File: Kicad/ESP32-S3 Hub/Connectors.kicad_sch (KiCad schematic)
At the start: 25 parts, among them J1 1.27mm 3pin socket, J10 1.27mm 3pin socket, J11 7 pin FPC 0.3mm Panasonic Y3b, J12 1.27mm 3pin socket, J13 TE 3-2363961-0 receptacle, J14 TE 3-2363962-0 Connector, J16 TE 3-2363961-0 receptacle, J17 TE 3-2363962-0 Connector, J2 1.27mm 3pin socket, J21 1.27mm 4 pin socket, J22 1.27mm 4 pin header, J3 7 pin FPC 0.3mm Panasonic Y3b, J4 1.27mm 3pin socket, J5 7 pin FPC 0.3mm Panasonic Y3b, J6 1.27mm 3pin socket, J7 1.27mm 3pin socket, J8 7 pin FPC 0.3mm Panasonic Y3b, J9 1.27mm 3pin socket

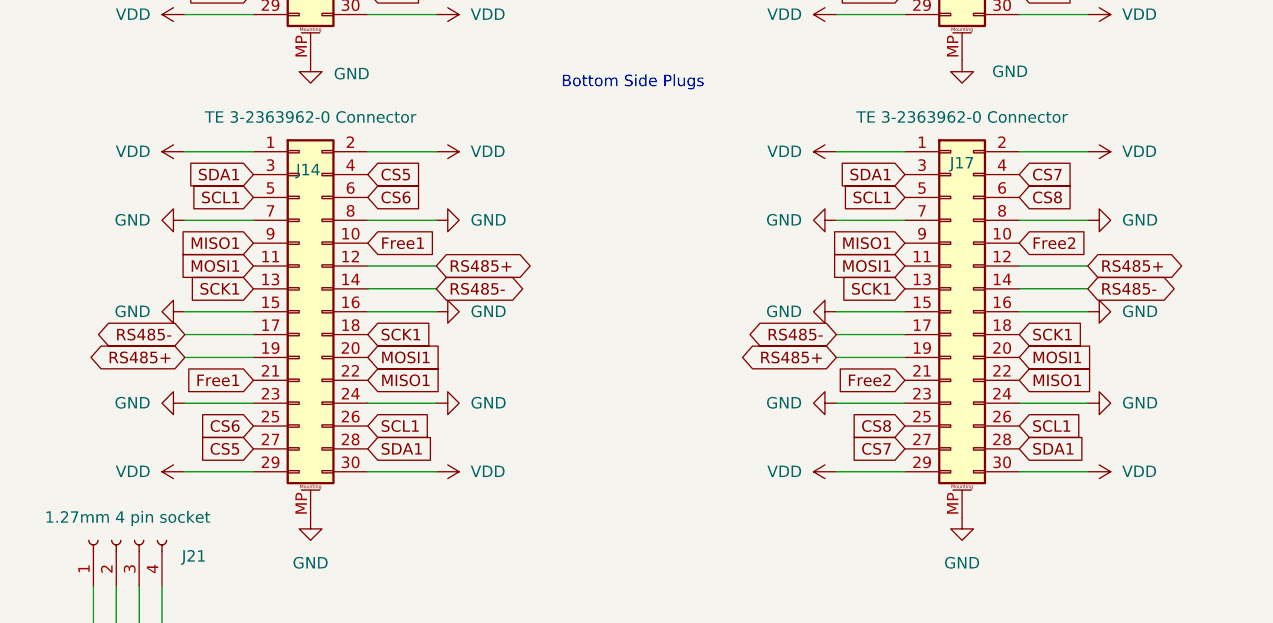
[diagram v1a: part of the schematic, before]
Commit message: Removed problem connections on bottom connector
We don't want several masters fighting over gpio pins or the SPI bus, so I have removed all connections on the bottom side except the multi-master capable busses.
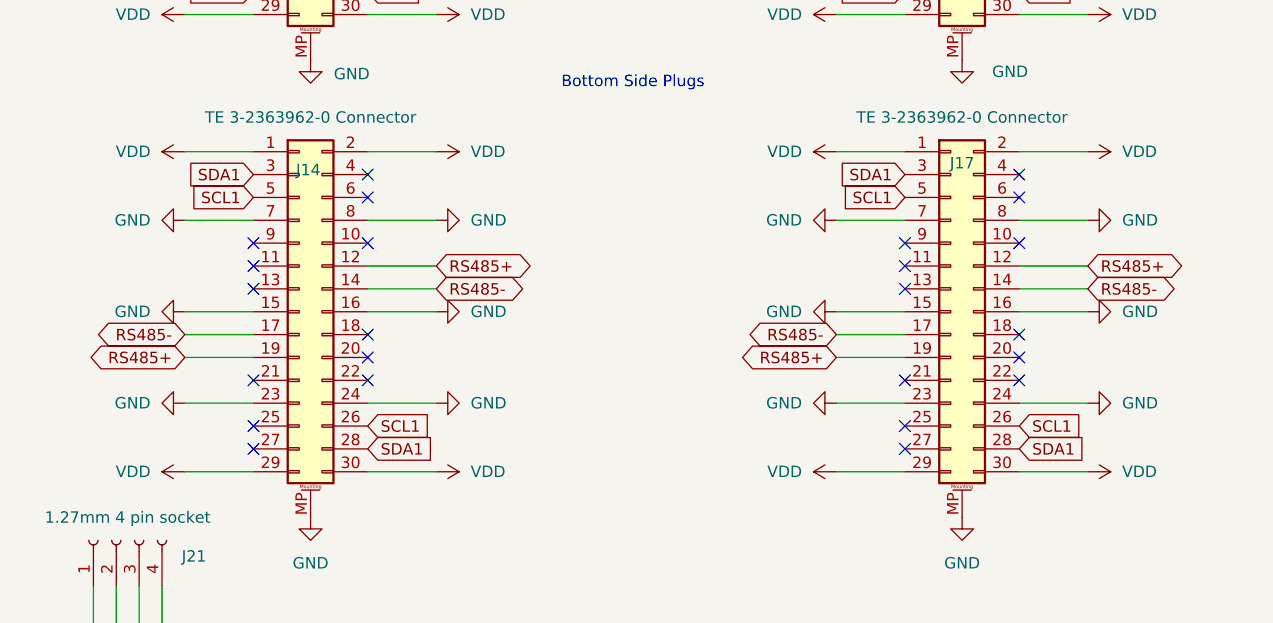
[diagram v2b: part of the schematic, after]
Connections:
- net CS5: no longer J14.27 (Pin_27), J14.4 (Pin_4)
- net CS6: no longer J14.25 (Pin_25), J14.6 (Pin_6)
- net CS7: no longer J17.27 (Pin_27), J17.4 (Pin_4)
- net CS8: no longer J17.25 (Pin_25), J17.6 (Pin_6)
- net Free1: no longer J14.10 (Pin_10), J14.21 (Pin_21)
- net Free2: no longer J17.10 (Pin_10), J17.21 (Pin_21)
- net MISO1: no longer J14.22 (Pin_22), J14.9 (Pin_9), J17.22 (Pin_22), J17.9 (Pin_9)
- net MOSI1: no longer J14.11 (Pin_11), J14.20 (Pin_20), J17.11 (Pin_11), J17.20 (Pin_20)
- net SCK1: no longer J14.13 (Pin_13), J14.18 (Pin_18), J17.13 (Pin_13), J17.18 (Pin_18)
- no-connect marks 4 -> 28

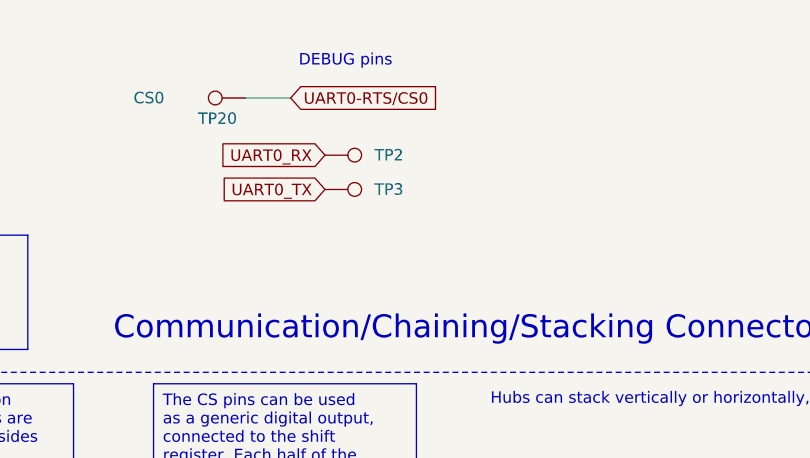
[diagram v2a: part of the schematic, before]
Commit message: Arranged Silkscreen
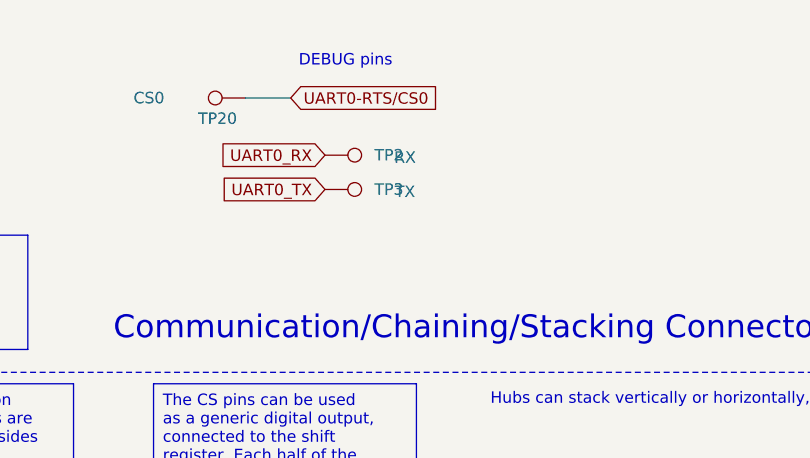
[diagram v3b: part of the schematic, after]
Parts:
- TP2: value ~ -> RX
- TP3: value ~ -> TX
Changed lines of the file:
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@@
 			)
 		)
-		(property "Value" "~"
+		(property "Value" "TX"
 			(at 207.01 32.004 90)
 			(effects
@@
 			)
 		)
-		(property "Value" "~"
+		(property "Value" "RX"
 			(at 207.01 28.194 90)
 			(effects

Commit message: Fixing board edge pin header 3d models
I tried first switching out the footprint entirely, but that resulted in the 3d models pointing in to the board. I rotated all the connections in the schematic and the board, but that came with a billion errors because the pin one is a square and way to many traces are close to the pins. I instead used my current vertical footprint and manually changed the 3d model for each. I may have problems if these headers are put in a pick and place, because they will point inward by default, but in most cases these should be hand soldered.
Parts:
- J1, J10, J12, J2, J4, J6, J7, J9: footprint Connector_PinHeader_1.27mm:PinHeader_1x03_P1.27mm_Vertical -> Connector_PinHeader_1.27mm:PinHeader_1x03_P1.27mm_Horizontal
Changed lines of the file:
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@@
 		(on_board yes)
 		(dnp no)
-		(fields_autoplaced yes)
 		(property "Reference" "J12"
 			(at 39.37 134.6199 0)
@@
 			)
 		)
-		(property "Footprint" "Connector_PinHeader_1.27mm:PinHeader_1x03_P1.27mm_Vertical"
+		(property "Footprint" "Connector_PinHeader_1.27mm:PinHeader_1x03_P1.27mm_Horizontal"
 			(at 38.1 135.89 0)
 			(effects
@@
 		(on_board yes)
 		(dnp no)
-		(fields_autoplaced yes)
 		(property "Reference" "J1"
 			(at 39.37 31.7499 0)
@@
 			)
 		)
-		(property "Footprint" "Connector_PinHeader_1.27mm:PinHeader_1x03_P1.27mm_Vertical"
+		(property "Footprint" "Connector_PinHeader_1.27mm:PinHeader_1x03_P1.27mm_Horizontal"
 			(at 38.1 33.02 0)
 			(effects
@@
 		(on_board yes)
 		(dnp no)
-		(fields_autoplaced yes)
 		(property "Reference" "J9"
 			(at 39.37 102.8699 0)
@@
 			)
 		)
-		(property "Footprint" "Connector_PinHeader_1.27mm:PinHeader_1x03_P1.27mm_Vertical"
+		(property "Footprint" "Connector_PinHeader_1.27mm:PinHeader_1x03_P1.27mm_Horizontal"
 			(at 38.1 104.14 0)
 			(effects
@@
 		(on_board yes)
 		(dnp no)
-		(fields_autoplaced yes)
 		(property "Reference" "J10"
 			(at 39.37 126.9999 0)
@@
 			)
 		)
-		(property "Footprint" "Connector_PinHeader_1.27mm:PinHeader_1x03_P1.27mm_Vertical"
+		(property "Footprint" "Connector_PinHeader_1.27mm:PinHeader_1x03_P1.27mm_Horizontal"
 			(at 38.1 128.27 0)
 			(effects
@@
 		(on_board yes)
 		(dnp no)
-		(fields_autoplaced yes)
 		(property "Reference" "J2"
 			(at 39.37 39.3699 0)
@@
 			)
 		)
-		(property "Footprint" "Connector_PinHeader_1.27mm:PinHeader_1x03_P1.27mm_Vertical"
+		(property "Footprint" "Connector_PinHeader_1.27mm:PinHeader_1x03_P1.27mm_Horizontal"
 			(at 38.1 40.64 0)
 			(effects
@@
 		(on_board yes)
 		(dnp no)
-		(fields_autoplaced yes)
 		(property "Reference" "J4"
 			(at 39.37 64.7699 0)
@@
 			)
 		)
-		(property "Footprint" "Connector_PinHeader_1.27mm:PinHeader_1x03_P1.27mm_Vertical"
+		(property "Footprint" "Connector_PinHeader_1.27mm:PinHeader_1x03_P1.27mm_Horizontal"
 			(at 38.1 66.04 0)
 			(effects
@@
 		(on_board yes)
 		(dnp no)
-		(fields_autoplaced yes)
 		(property "Reference" "J6"
 			(at 39.37 72.3899 0)
@@
 			)
 		)
-		(property "Footprint" "Connector_PinHeader_1.27mm:PinHeader_1x03_P1.27mm_Vertical"
+		(property "Footprint" "Connector_PinHeader_1.27mm:PinHeader_1x03_P1.27mm_Horizontal"
 			(at 38.1 73.66 0)
 			(effects
@@
 		(on_board yes)
 		(dnp no)
-		(fields_autoplaced yes)
 		(property "Reference" "J7"
 			(at 39.37 95.2499 0)
@@
 			)
 		)
-		(property "Footprint" "Connector_PinHeader_1.27mm:PinHeader_1x03_P1.27mm_Vertical"
+		(property "Footprint" "Connector_PinHeader_1.27mm:PinHeader_1x03_P1.27mm_Horizontal"
 			(at 38.1 96.52 0)
 			(effects

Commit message: Fixed OE pin by adding pullup, updated silkscreen
The silkscreen looks really nice now, I have all the port labels.
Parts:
- J1, J10, J12, J2, J4, J6, J7, J9: footprint Connector_PinHeader_1.27mm:PinHeader_1x03_P1.27mm_Horizontal -> Connector_PinHeader_1.27mm:PinHeader_1x03_P1.27mm_Vertical
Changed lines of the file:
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@@
 			)
 		)
-		(property "Footprint" "Connector_PinHeader_1.27mm:PinHeader_1x03_P1.27mm_Horizontal"
+		(property "Footprint" "Connector_PinHeader_1.27mm:PinHeader_1x03_P1.27mm_Vertical"
 			(at 38.1 135.89 0)
 			(effects
@@
 			)
 		)
-		(property "Footprint" "Connector_PinHeader_1.27mm:PinHeader_1x03_P1.27mm_Horizontal"
+		(property "Footprint" "Connector_PinHeader_1.27mm:PinHeader_1x03_P1.27mm_Vertical"
 			(at 38.1 33.02 0)
 			(effects
@@
 			)
 		)
-		(property "Footprint" "Connector_PinHeader_1.27mm:PinHeader_1x03_P1.27mm_Horizontal"
+		(property "Footprint" "Connector_PinHeader_1.27mm:PinHeader_1x03_P1.27mm_Vertical"
 			(at 38.1 104.14 0)
 			(effects
@@
 			)
 		)
-		(property "Footprint" "Connector_PinHeader_1.27mm:PinHeader_1x03_P1.27mm_Horizontal"
+		(property "Footprint" "Connector_PinHeader_1.27mm:PinHeader_1x03_P1.27mm_Vertical"
 			(at 38.1 128.27 0)
 			(effects
@@
 			)
 		)
-		(property "Footprint" "Connector_PinHeader_1.27mm:PinHeader_1x03_P1.27mm_Horizontal"
+		(property "Footprint" "Connector_PinHeader_1.27mm:PinHeader_1x03_P1.27mm_Vertical"
 			(at 38.1 40.64 0)
 			(effects
@@
 			)
 		)
-		(property "Footprint" "Connector_PinHeader_1.27mm:PinHeader_1x03_P1.27mm_Horizontal"
+		(property "Footprint" "Connector_PinHeader_1.27mm:PinHeader_1x03_P1.27mm_Vertical"
 			(at 38.1 66.04 0)
 			(effects
@@
 			)
 		)
-		(property "Footprint" "Connector_PinHeader_1.27mm:PinHeader_1x03_P1.27mm_Horizontal"
+		(property "Footprint" "Connector_PinHeader_1.27mm:PinHeader_1x03_P1.27mm_Vertical"
 			(at 38.1 73.66 0)
 			(effects
@@
 			)
 		)
-		(property "Footprint" "Connector_PinHeader_1.27mm:PinHeader_1x03_P1.27mm_Horizontal"
+		(property "Footprint" "Connector_PinHeader_1.27mm:PinHeader_1x03_P1.27mm_Vertical"
 			(at 38.1 96.52 0)
 			(effects

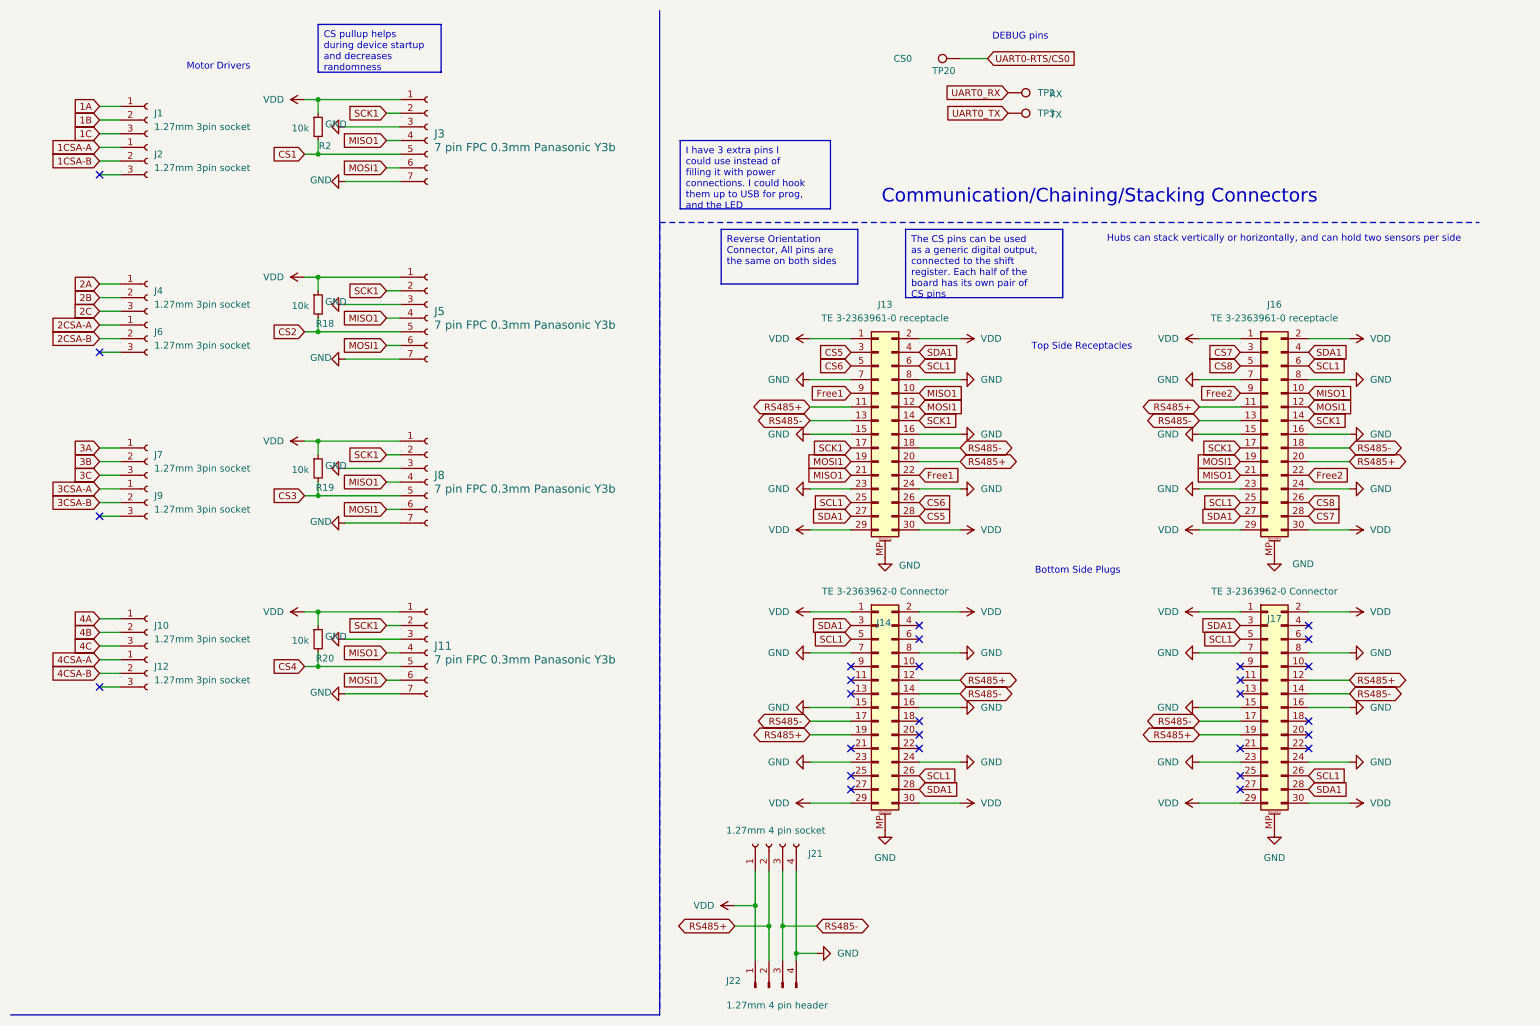
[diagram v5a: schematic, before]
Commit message: Added LCSC part numbers, DNP attr, and exported Gerbers
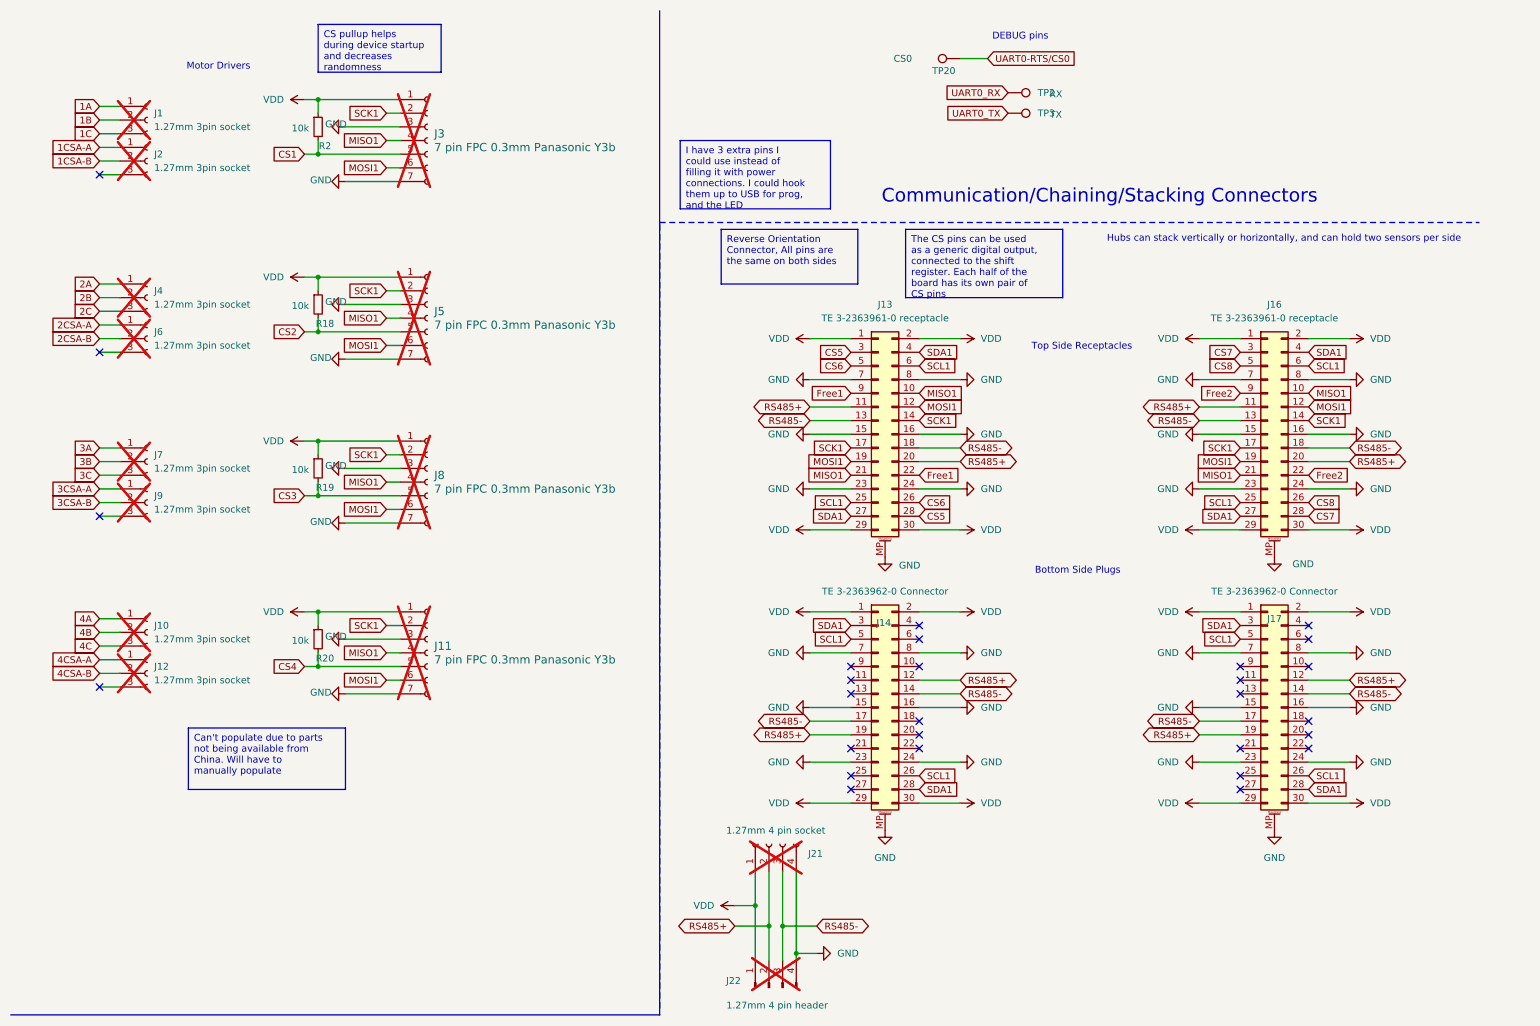
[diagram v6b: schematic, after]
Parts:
- J1, J10, J11, J12, J2, J21, J22, J3, J4, J5, J6, J7, J8, J9: now not fitted
- J13, J16: LCSC (none) -> C425103
- J14, J17: LCSC (none) -> C425104
- R18, R19, R2, R20: LCSC (none) -> C25744
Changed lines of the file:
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@@
 		)
 	)
+	(text_box "Can't populate due to parts not being available from China. Will have to manually populate"
+		(exclude_from_sim no)
+		(at 45.72 146.05 0)
+		(size 29.21 11.43)
+		(stroke
+			(width 0)
+			(type default)
+		)
+		(fill
+			(type none)
+		)
+		(effects
+			(font
+				(size 1.27 1.27)
+			)
+			(justify left top)
+		)
+	)
 	(text_box "The CS pins can be used as a generic digital output, connected to the shift register. Each half of the board has its own pair of CS pins"
 		(exclude_from_sim no)
@@
 		(in_bom yes)
 		(on_board yes)
-		(dnp no)
+		(dnp yes)
 		(property "Reference" "J12"
 			(at 39.37 134.6199 0)
@@
 		(in_bom yes)
 		(on_board yes)
-		(dnp no)
+		(dnp yes)
 		(property "Reference" "J1"
 			(at 39.37 31.7499 0)
@@
 		(in_bom yes)
 		(on_board yes)
-		(dnp no)
+		(dnp yes)
 		(property "Reference" "J9"
 			(at 39.37 102.8699 0)
@@
 		(in_bom yes)
 		(on_board yes)
-		(dnp no)
+		(dnp yes)
 		(fields_autoplaced yes)
 		(property "Reference" "J5"
@@
 			)
 		)
+		(property "LCSC" "C25744"
+			(at 71.12 133.096 0)
+			(effects
+				(font
+					(size 1.27 1.27)
+				)
+				(hide yes)
+			)
+		)
 		(pin "2"
 		)
@@
 		(in_bom yes)
 		(on_board yes)
-		(dnp no)
+		(dnp yes)
 		(property "Reference" "J10"
 			(at 39.37 126.9999 0)
@@
 		(in_bom yes)
 		(on_board yes)
-		(dnp no)
+		(dnp yes)
 		(property "Reference" "J2"
 			(at 39.37 39.3699 0)
@@
 			)
 		)
+		(property "LCSC" "C425104"
+			(at 175.006 126.492 0)
+			(effects
+				(font
+					(size 1.27 1.27)
+				)
+				(hide yes)
+			)
+		)
 		(pin "28"
 		)
@@
 			)
 		)
+		(property "LCSC" "C25744"
+			(at 71.12 101.346 0)
+			(effects
+				(font
+					(size 1.27 1.27)
+				)
+				(hide yes)
+			)
+		)
 		(pin "2"
 		)
@@
 			)
 		)
+		(property "LCSC" "C425104"
+			(at 247.65 125.73 0)
+			(effects
+				(font
+					(size 1.27 1.27)
+				)
+				(hide yes)
+			)
+		)
 		(pin "28"
 		)
@@
 		(in_bom yes)
 		(on_board yes)
-		(dnp no)
+		(dnp yes)
 		(fields_autoplaced yes)
 		(property "Reference" "J3"
@@
 			)
 		)
+		(property "LCSC" "C425103"
+			(at 175.26 67.31 0)
+			(effects
+				(font
+					(size 1.27 1.27)
+				)
+				(hide yes)
+			)
+		)
 		(pin "28"
 		)
@@
 		(in_bom yes)
 		(on_board yes)
-		(dnp no)
+		(dnp yes)
 		(property "Reference" "J21"
 			(at 162.306 169.418 90)
@@
 		(in_bom yes)
 		(on_board yes)
-		(dnp no)
+		(dnp yes)
 		(fields_autoplaced yes)
 		(property "Reference" "J11"
@@
 			)
 		)
+		(property "LCSC" "C25744"
+			(at 71.12 70.866 0)
+			(effects
+				(font
+					(size 1.27 1.27)
+				)
+				(hide yes)
+			)
+		)
 		(pin "2"
 		)
@@
 		(in_bom yes)
 		(on_board yes)
-		(dnp no)
+		(dnp yes)
 		(property "Reference" "J4"
 			(at 39.37 64.7699 0)
@@
 		(in_bom yes)
 		(on_board yes)
-		(dnp no)
+		(dnp yes)
 		(property "Reference" "J6"
 			(at 39.37 72.3899 0)
@@
 		(in_bom yes)
 		(on_board yes)
-		(dnp no)
+		(dnp yes)
 		(property "Reference" "J7"
 			(at 39.37 95.2499 0)
@@
 		(in_bom yes)
 		(on_board yes)
-		(dnp no)
+		(dnp yes)
 		(fields_autoplaced yes)
 		(property "Reference" "J8"
@@
 		(in_bom yes)
 		(on_board yes)
-		(dnp no)
+		(dnp yes)
 		(property "Reference" "J22"
 			(at 147.066 193.04 90)
@@
 			)
 		)
+		(property "LCSC" "C425103"
+			(at 247.65 67.31 0)
+			(effects
+				(font
+					(size 1.27 1.27)
+				)
+				(hide yes)
+			)
+		)
 		(pin "28"
 		)
@@
 			(effects
 				(font
+					(size 1.27 1.27)
+				)
+				(hide yes)
+			)
+		)
+		(property "LCSC" "C25744"
+			(at 71.12 37.846 0)
+			(effects
+				(font
